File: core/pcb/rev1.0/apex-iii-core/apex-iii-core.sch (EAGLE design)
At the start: 68 parts

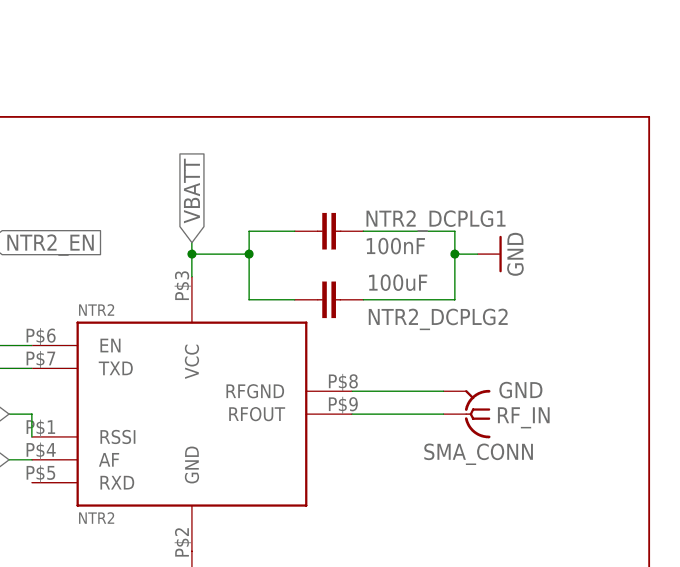
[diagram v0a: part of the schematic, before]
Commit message: setup module folders
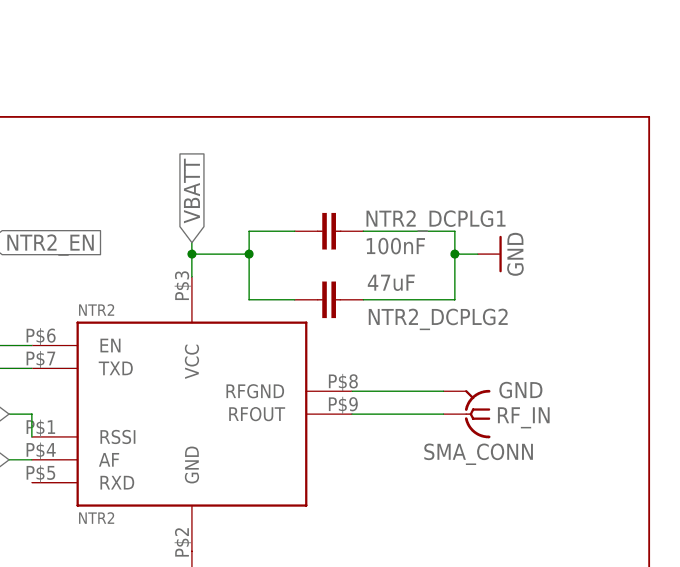
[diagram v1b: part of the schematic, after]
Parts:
- NTR2_DCPLG2: value 100uF -> 47uF
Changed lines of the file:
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@@
 <part name="GPS_DCPLG" library="SparkFun" deviceset="CAP" device="0805" value="100nF"/>
 <part name="GND18" library="SparkFun" deviceset="GND" device=""/>
-<part name="NTR2_DCPLG2" library="SparkFun" deviceset="CAP" device="0805" value="100uF"/>
+<part name="NTR2_DCPLG2" library="SparkFun" deviceset="CAP" device="0805" value="47uF"/>
 <part name="GND19" library="SparkFun" deviceset="GND" device=""/>
 <part name="GND20" library="SparkFun" deviceset="GND" device=""/>
